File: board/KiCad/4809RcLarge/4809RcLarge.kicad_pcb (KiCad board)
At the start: 2 copper layers, 20.7 x 41.1 mm, 34 parts, among them J1 `, J2 Conn_01x06_Male, J3 Conn_01x16_Male, Q1 Q_NMOS_GSD, Q2 Q_NMOS_GSD, Q3 Q_NMOS_GSD, Q4 Q_NMOS_GSD, Q5 Q_NMOS_GSD, Q6 Q_NMOS_GSD, U1 ATmega4809-A

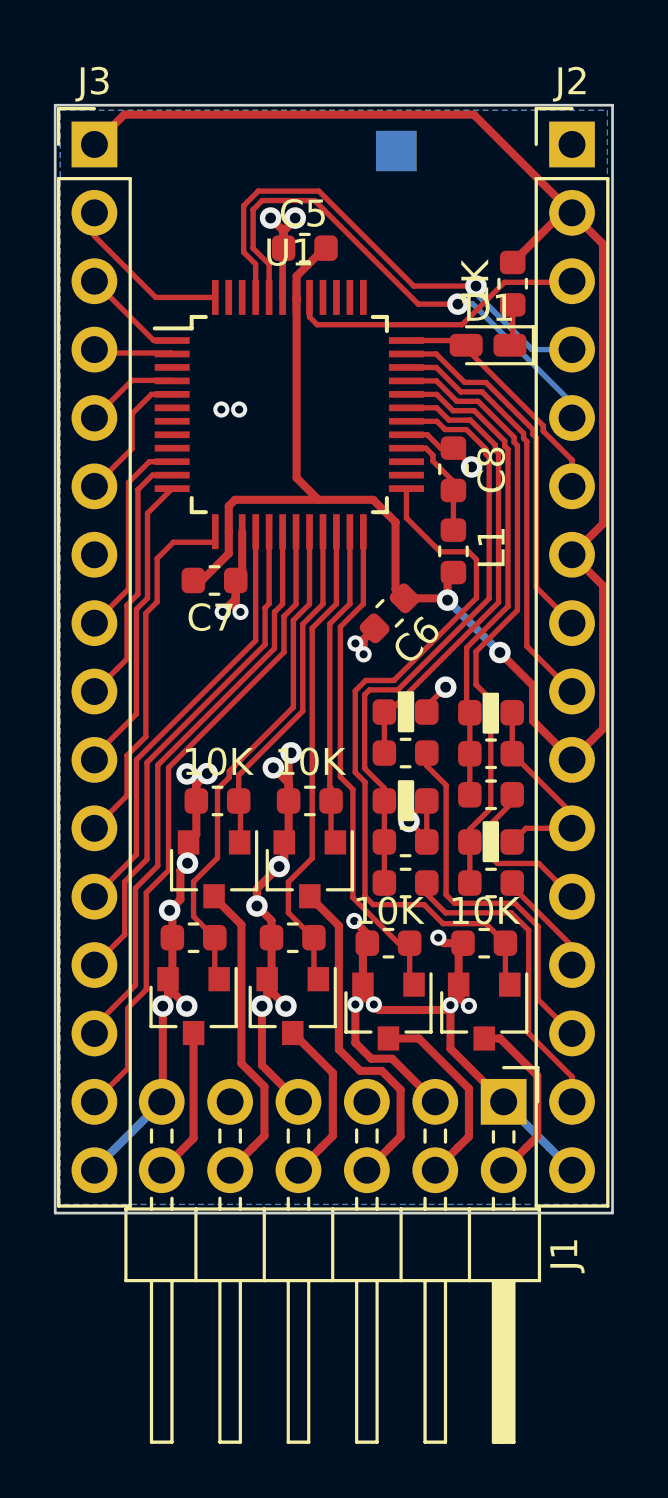
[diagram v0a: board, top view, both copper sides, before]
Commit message: Finished Large (standard 2.54 pitch pins) board using quad flat pack version of 4809. Added a quad flat pack version of the 'sm' board (not quite as small), the no lead (UQFN) version has had a lot of issues with dead pins (not really meant for 'home use'). Both of these also pull out a bunch more pins to 'test pads' these are obviously not nearly as good as real pads but would be way better than trying to solder to a lead in a pinch.
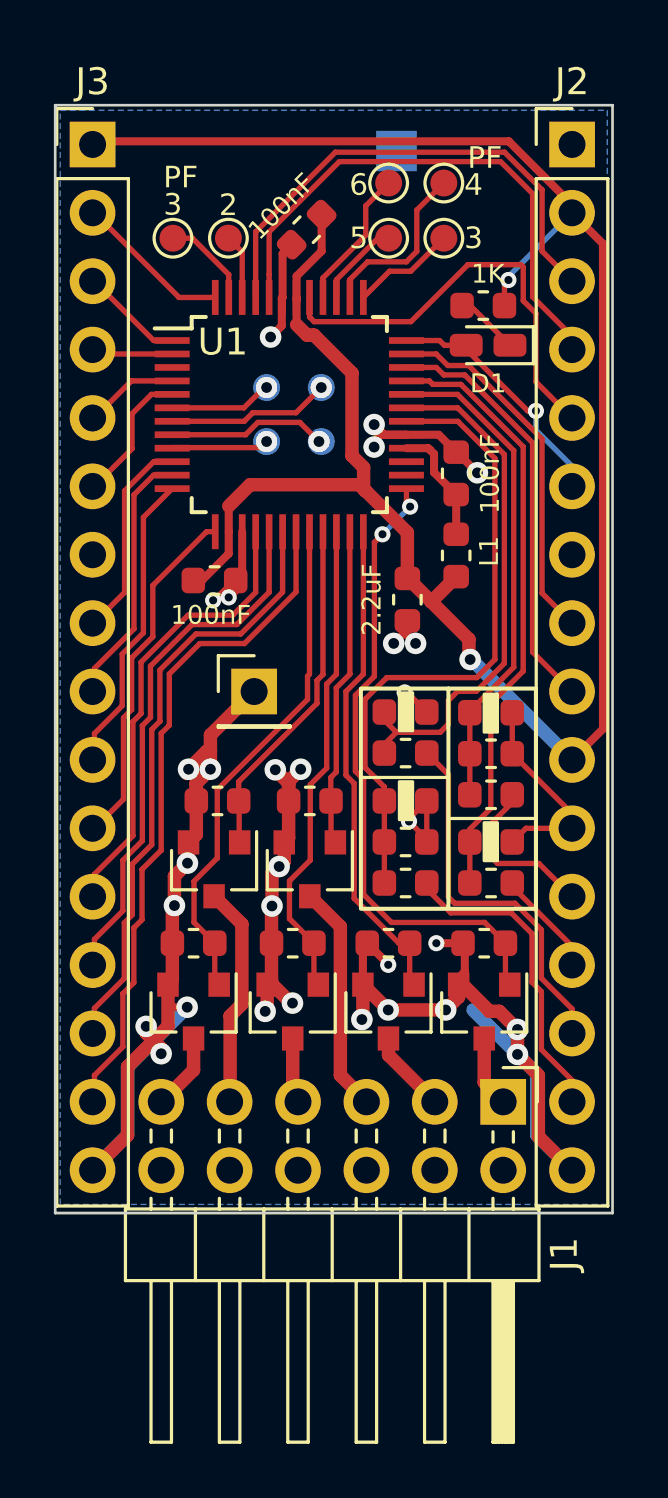
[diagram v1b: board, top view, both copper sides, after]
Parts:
- removed C5, C6: 100nF, Capacitor_SMD:C_0603_1608Metric
- added 100nF: 100nF, Capacitor_SMD:C_0603_1608Metric, F.Cu at (170.9, 61.2)
- added 2.2uF: 100nF, Capacitor_SMD:C_0603_1608Metric, F.Cu at (174.7, 74.9)
- added J4: Conn_01x01_Male, Connector_PinHeader_2.54mm:PinHeader_1x01_P2.54mm_Vertical, F.Cu at (169.0, 78.4)
- added TP10: TestPoint, TestPoint:TestPoint_Pad_D1.0mm, F.Cu at (168.0, 61.5)
- added TP11: TestPoint, TestPoint:TestPoint_Pad_D1.0mm, F.Cu at (166.0, 61.5)
- added TP2: TestPoint, TestPoint:TestPoint_Pad_D1.0mm, B.Cu at (171.5, 67.1)
- added TP3: TestPoint, TestPoint:TestPoint_Pad_D1.0mm, B.Cu at (171.5, 69.1)
- added TP4: TestPoint, TestPoint:TestPoint_Pad_D1.0mm, B.Cu at (169.5, 69.1)
- added TP5: TestPoint, TestPoint:TestPoint_Pad_D1.0mm, B.Cu at (169.5, 67.1)
- added TP6: TestPoint, TestPoint:TestPoint_Pad_D1.0mm, F.Cu at (176.0, 61.5)
- added TP7: TestPoint, TestPoint:TestPoint_Pad_D1.0mm, F.Cu at (176.0, 59.5)
- added TP8: TestPoint, TestPoint:TestPoint_Pad_D1.0mm, F.Cu at (174.0, 61.5)
- added TP9: TestPoint, TestPoint:TestPoint_Pad_D1.0mm, F.Cu at (174.0, 59.5)
- moved R13 1.36 mm to (177.5, 64.0), turned to 0 degrees
- moved Q1 0.20 mm to (166.8, 90.2)
- moved Q5 0.20 mm to (170.4, 90.2)
- moved R1 0.20 mm to (166.8, 87.7)
- moved R7 0.20 mm to (170.4, 87.7)
- moved 100nF 0.18 mm to (176.5, 70.3)
- moved L1 0.18 mm to (176.5, 73.3)
- moved J3 0.07 mm to (163.0, 58.0)
- renumbered C7 to 100nF, C8 to 100nF
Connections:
- J1 pad 1: GND -> Net-(J1-Pad1)
- J1 pad 10: Net-(J1-Pad10) -> VCC
- J1 pad 11: GND -> Net-(J1-Pad11)
- J1 pad 12: Net-(J1-Pad12) -> VCC
- J1 pad 2: Net-(J1-Pad2) -> VCC
- J1 pad 3: GND -> Net-(J1-Pad3)
- J1 pad 4: Net-(J1-Pad4) -> VCC
- J1 pad 5: GND -> Net-(J1-Pad5)
- J1 pad 6: Net-(J1-Pad6) -> VCC
- J1 pad 7: GND -> Net-(J1-Pad7)
- J1 pad 8: Net-(J1-Pad8) -> VCC
- J1 pad 9: GND -> Net-(J1-Pad9)
- Q1 pad 3: Net-(J1-Pad12) -> Net-(J1-Pad11)
- Q2 pad 3: Net-(J1-Pad6) -> Net-(J1-Pad5)
- Q3 pad 3: Net-(J1-Pad4) -> Net-(J1-Pad3)
- Q4 pad 3: Net-(J1-Pad10) -> Net-(J1-Pad9)
- Q5 pad 3: Net-(J1-Pad8) -> Net-(J1-Pad7)
- Q6 pad 3: Net-(J1-Pad2) -> Net-(J1-Pad1)
- U1 pad 37: (no net) -> Net-(TP6-Pad1)
- U1 pad 38: (no net) -> Net-(TP7-Pad1)
- U1 pad 39: (no net) -> Net-(TP8-Pad1)
- U1 pad 40: (no net) -> Net-(TP9-Pad1)
- U1 pad 41: Net-(J2-Pad3) -> Net-(J2-Pad5)
- U1 pad 44: Net-(J2-Pad5) -> Net-(J2-Pad4)
- U1 pad 45: Net-(J2-Pad4) -> Net-(J2-Pad3)
- U1 pad 46: (no net) -> Net-(TP10-Pad1)
- U1 pad 47: (no net) -> Net-(TP11-Pad1)
- U1 pad 6: (no net) -> Net-(TP5-Pad1)
- U1 pad 7: (no net) -> Net-(TP2-Pad1)
- U1 pad 8: (no net) -> Net-(TP3-Pad1)
- U1 pad 9: (no net) -> Net-(TP4-Pad1)
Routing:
- net GND: track 87.7 -> 101.0 mm, vias 29 -> 30
- net Net-(J1-Pad6): track 12.6 -> 0.00 mm
- net Net-(J1-Pad10): track 11.5 -> 0.00 mm
- net Net-(J1-Pad5): track 0.00 -> 8.52 mm
- net Net-(J1-Pad9): track 0.00 -> 8.24 mm
- net Net-(J2-Pad3): track 11.3 -> 18.7 mm
- net Net-(J1-Pad4): track 7.31 -> 0.00 mm
- net Net-(J1-Pad2): track 6.58 -> 0.00 mm
- net Net-(TP7-Pad1): track 0.00 -> 6.54 mm
- net Net-(J1-Pad8): track 6.25 -> 0.00 mm
- net Net-(TP2-Pad1): track 0.00 -> 6.06 mm, vias 0 -> 1
- net Net-(TP3-Pad1): track 0.00 -> 5.94 mm, vias 0 -> 1
- net Net-(J1-Pad12): track 5.59 -> 0.00 mm
- net Net-(TP9-Pad1): track 0.00 -> 5.26 mm
- net Net-(TP6-Pad1): track 0.00 -> 3.90 mm
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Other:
- rule pad_to_mask_clearance: 0.051 -> 0
